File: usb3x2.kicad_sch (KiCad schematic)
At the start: 90 parts

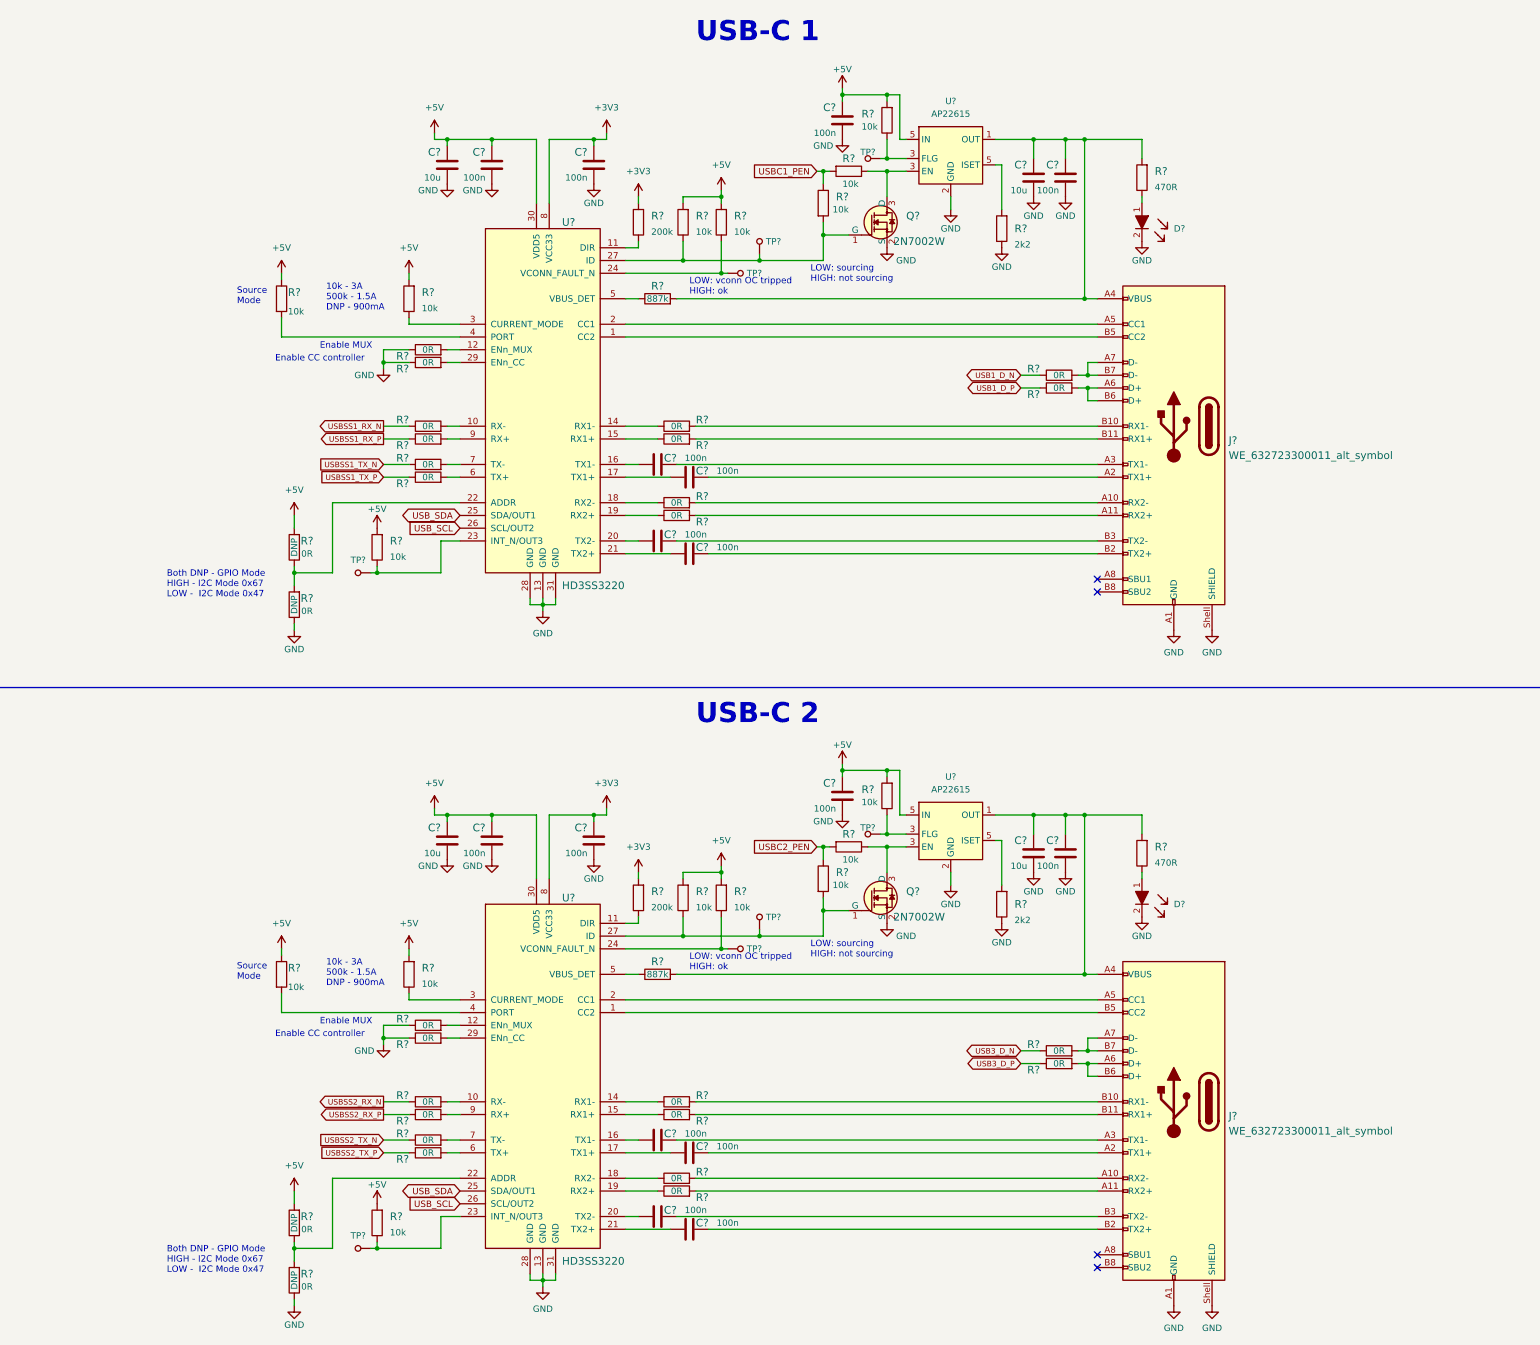
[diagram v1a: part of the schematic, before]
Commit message: Added ESD protection for USB connectors
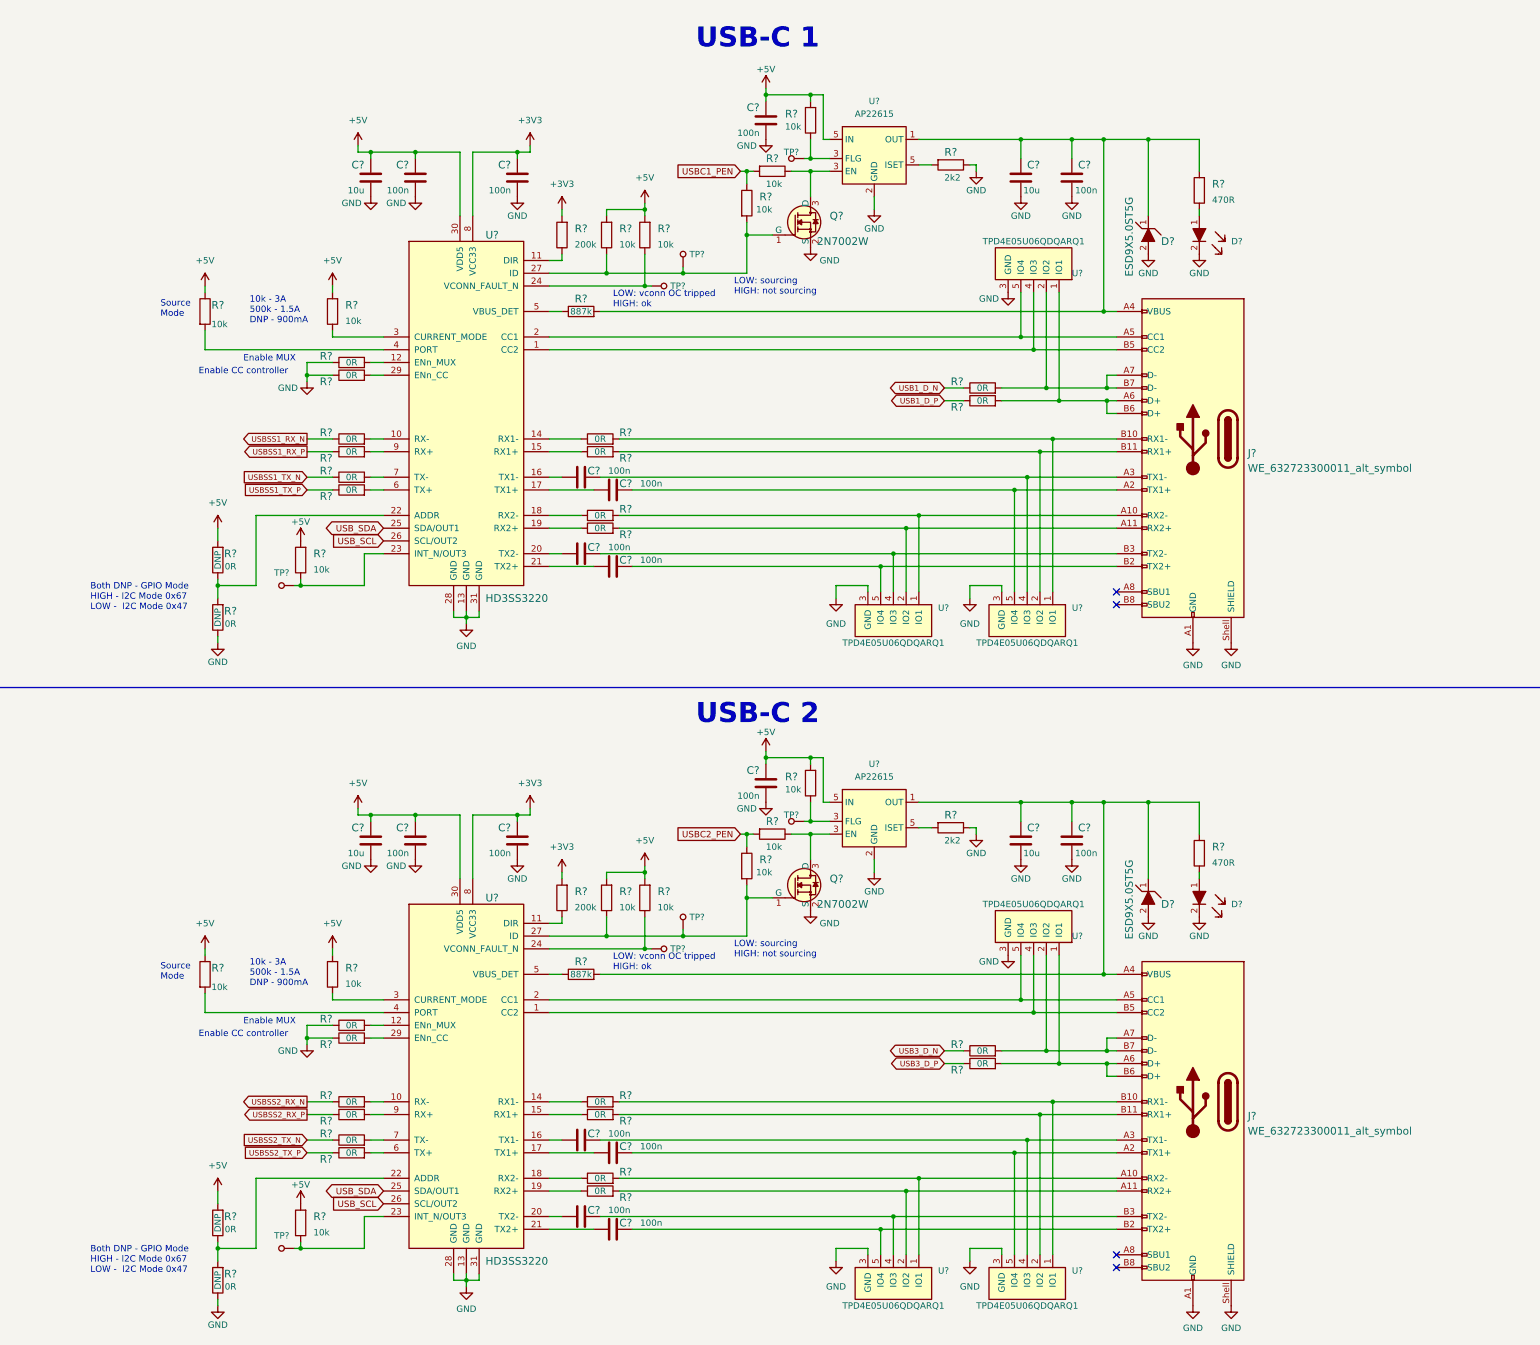
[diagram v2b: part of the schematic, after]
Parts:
- removed C? (x8): C_100n_0402, antmicro-footprints:0402-cap, symbol antmicroCapacitors0402:C_100n_0402
- removed C? (x2): C_10u_0603, antmicro-footprints:0603-cap, symbol antmicroCapacitors0603:C_10u_0603
- removed D?: LTST-C190GKT, crosslink-nx-video-converter-footprints:LED_0603, symbol crosslink-nx-video-converter:LTST-C190GKT
- removed J?: WE_632723300011_alt_symbol, antmicro-footprints:WE_632723300011, symbol antmicroUSBDVIHDMIConnectors:WE_632723300011_alt_symbol
- removed Q?: 2N7002W, antmicro-footprints:SOT-323, symbol antmicroTransistorsFETsMOSFETsSingle: 2N7002W
- removed R? (x8): R_10k_0402, antmicro-footprints:0402-res, symbol antmicroResistors0402:R_10k_0402
- removed R? (x14): R_0R_0402, antmicro-footprints:0402-res, symbol antmicroResistors0402:R_0R_0402
- removed R?: R_470R_0603, antmicro-footprints:0603-res, symbol antmicroResistors0603:R_470R_0603
- removed R?: R_2k2_0402, antmicro-footprints:0402-res, symbol antmicroResistors0402:R_2k2_0402
- removed R?: R_200k_0402, antmicro-footprints:0402-res, symbol antmicroResistors0402:R_200k_0402
- removed R?: R_887k_0402, antmicro-footprints:0402-res, symbol antmicroResistors0402:R_887k_0402
- removed TP? (x4): TP_SMD_0_75MM, antmicro-footprints:Testpoint_smd_0_75mm, symbol antmicroTestPoints:TP_SMD_0_75MM
- removed U?: HD3SS3220, antmicro-footprints:RNH0030A, symbol antmicroInterfaceControllers:HD3SS3220
- removed U?: AP22615, antmicro-footprints:TSOT23-6, symbol antmicroPMICPowerDistributionSwitchesLoadDrivers:AP22615
- added C? (x2): C_10u_0603, antmicro-footprints:0603-cap, symbol antmicroCapacitors0603:C_10u_0603
- added C? (x8): C_100n_0402, antmicro-footprints:0402-cap, symbol antmicroCapacitors0402:C_100n_0402
- added D?: LTST-C190GKT, crosslink-nx-video-converter-footprints:LED_0603, symbol crosslink-nx-video-converter:LTST-C190GKT
- added D? (x2): ESD9X5.0ST5G, antmicro-footprints:SOD-923, symbol antmicroTVSDiodes:ESD9X5.0ST5G
- added J?: WE_632723300011_alt_symbol, antmicro-footprints:WE_632723300011, symbol antmicroUSBDVIHDMIConnectors:WE_632723300011_alt_symbol
- added Q?: 2N7002W, antmicro-footprints:SOT-323, symbol antmicroTransistorsFETsMOSFETsSingle: 2N7002W
- added R? (x14): R_0R_0402, antmicro-footprints:0402-res, symbol antmicroResistors0402:R_0R_0402
- added R?: R_470R_0603, antmicro-footprints:0603-res, symbol antmicroResistors0603:R_470R_0603
- added R? (x8): R_10k_0402, antmicro-footprints:0402-res, symbol antmicroResistors0402:R_10k_0402
- added R?: R_200k_0402, antmicro-footprints:0402-res, symbol antmicroResistors0402:R_200k_0402
- added R?: R_2k2_0402, antmicro-footprints:0402-res, symbol antmicroResistors0402:R_2k2_0402
- added R?: R_887k_0402, antmicro-footprints:0402-res, symbol antmicroResistors0402:R_887k_0402
- added TP? (x4): TP_SMD_0_75MM, antmicro-footprints:Testpoint_smd_0_75mm, symbol antmicroTestPoints:TP_SMD_0_75MM
- added U?: HD3SS3220, antmicro-footprints:RNH0030A, symbol antmicroInterfaceControllers:HD3SS3220
- added U?: AP22615, antmicro-footprints:TSOT23-6, symbol antmicroPMICPowerDistributionSwitchesLoadDrivers:AP22615
- added U? (x6): TPD4E05U06QDQARQ1, antmicro-footprints:TPD4E05U06QDQARQ1, symbol antmicroTVSDiodes:TPD4E05U06QDQARQ1
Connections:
- net +3V3: now also C?.1, R?.2, U?.8 (VCC33)
- net +5V: now also C?.1, C?.1, C?.1, R?.1, R?.2, R?.2, R?.2, R?.2, R?.2, R?.2, U?.30 (VDD5), U?.5 (ISET)
- net GND: now also C?.2, C?.2, C?.2, C?.2, C?.2, C?.2, D?.2, D?.2, D?.2, J?.A1 (GND), J?.A12 (GND), J?.B1 (GND), J?.B12 (GND), J?.Shell (SHIELD), Q?.2 (S), R?.1, R?.1, R?.1, R?.1, U?.13 (GND), U?.2 (GND), U?.28 (GND), U?.3 (GND), U?.3 (GND), U?.3 (GND), U?.3 (GND), U?.3 (GND), U?.3 (GND), U?.31 (GND), U?.8 (GND), U?.8 (GND), U?.8 (GND), U?.8 (GND), U?.8 (GND), U?.8 (GND)
- net USB1_D_N: now also R?.1
- net USB1_D_P: now also R?.1
- net USBC1_PEN: now also R?.1, R?.2
- net USBSS1_RX_N: now also R?.1
- net USBSS1_RX_P: now also R?.1
- net USBSS1_TX_N: now also R?.1
- net USBSS1_TX_P: now also R?.1
- net USB_SCL: now also U?.26 (SCL/OUT2)
- net USB_SDA: now also U?.25 (SDA/OUT1)
- net at C?.1, C?.1, J?.A4 (VBUS)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: now also D?.1
- net at C?.2, J?.B2 (TX2+): now also U?.5 (IO4), U?.6 (IO4)
- net at J?.A7 (D-), J?.B7 (D-), R?.2: now also U?.2 (IO2), U?.9 (IO2)
- net at J?.B5 (CC2), U?.1 (CC2): now also U?.4 (IO3), U?.7 (IO3)
- net at J?.A5 (CC1), U?.2 (CC1): now also U?.5 (IO4), U?.6 (IO4)
- net at C?.2, J?.A2 (TX1+): now also U?.5 (IO4), U?.6 (IO4)
- net at J?.A10 (RX2-), R?.2: now also U?.1 (IO1), U?.10 (IO1)
- net at J?.B11 (RX1+), R?.2: now also U?.2 (IO2), U?.9 (IO2)
- net at C?.2, J?.B3 (TX2-): now also U?.4 (IO3), U?.7 (IO3)
- net at C?.2, J?.A3 (TX1-): now also U?.4 (IO3), U?.7 (IO3)
- net at J?.A11 (RX2+), R?.2: now also U?.2 (IO2), U?.9 (IO2)
- net at J?.A6 (D+), J?.B6 (D+), R?.2: now also U?.1 (IO1), U?.10 (IO1)
- net at J?.B10 (RX1-), R?.2: now also U?.1 (IO1), U?.10 (IO1)
- new net: J?.B5 (CC2), U?.1 (CC2), U?.4 (IO3), U?.7 (IO3)
- new net: R?.2, U?.10 (RX-)
- new net: R?.1, U?.11 (DIR)
- new net: R?.2, U?.12 (ENn_MUX)
- new net: R?.1, U?.14 (RX1-)
- new net: R?.1, U?.15 (RX1+)
- new net: C?.1, U?.16 (TX1-)
- new net: C?.1, U?.17 (TX1+)
- new net: R?.1, U?.18 (RX2-)
- new net: R?.1, U?.19 (RX2+)
- new net: J?.A5 (CC1), U?.2 (CC1), U?.5 (IO4), U?.6 (IO4)
- new net: C?.1, U?.20 (TX2-)
- new net: C?.1, U?.21 (TX2+)
- new net: R?.1, R?.2, U?.22 (ADDR)
- new net: R?.1, TP?.1, U?.23 (INT_N/OUT3)
- new net: R?.1, TP?.1, U?.24 (VCONN_FAULT_N)
- new net: Q?.1 (G), R?.1, R?.2, TP?.1, U?.27 (ID)
- new net: R?.2, U?.29 (ENn_CC)
- new net: R?.1, U?.3 (CURRENT_MODE)
- new net: R?.2, U?.4 (PORT)
- new net: R?.1, U?.5 (VBUS_DET)
- new net: R?.2, U?.6 (TX+)
- new net: R?.2, U?.7 (TX-)
- new net: R?.2, U?.9 (RX+)
- new net: J?.A10 (RX2-), R?.2, U?.1 (IO1), U?.10 (IO1)
- new net: D?.1, R?.1
- new net: C?.1, C?.1, D?.1, J?.A4 (VBUS), J?.A9 (VBUS), J?.B4 (VBUS), J?.B9 (VBUS), R?.2, R?.2, U?.1 (OUT)
- new net: R?.1, TP?.1, U?.3 (FLG)
- new net: Q?.3 (D), R?.1, U?.3 (FLG)
- new net: R?.2, U?.5 (ISET)
- new net: J?.A6 (D+), J?.B6 (D+), R?.2, U?.1 (IO1), U?.10 (IO1)
- new net: C?.2, J?.A2 (TX1+), U?.5 (IO4), U?.6 (IO4)
- new net: J?.A11 (RX2+), R?.2, U?.2 (IO2), U?.9 (IO2)
- new net: C?.2, J?.B3 (TX2-), U?.4 (IO3), U?.7 (IO3)
- new net: C?.2, J?.B2 (TX2+), U?.5 (IO4), U?.6 (IO4)
- new net: C?.2, J?.A3 (TX1-), U?.4 (IO3), U?.7 (IO3)
- new net: J?.A7 (D-), J?.B7 (D-), R?.2, U?.2 (IO2), U?.9 (IO2)
- new net: J?.B10 (RX1-), R?.2, U?.1 (IO1), U?.10 (IO1)
- new net: J?.B11 (RX1+), R?.2, U?.2 (IO2), U?.9 (IO2)
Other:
- moved on the sheet: C?, D?, J?, Q?, R?, TP?, U?

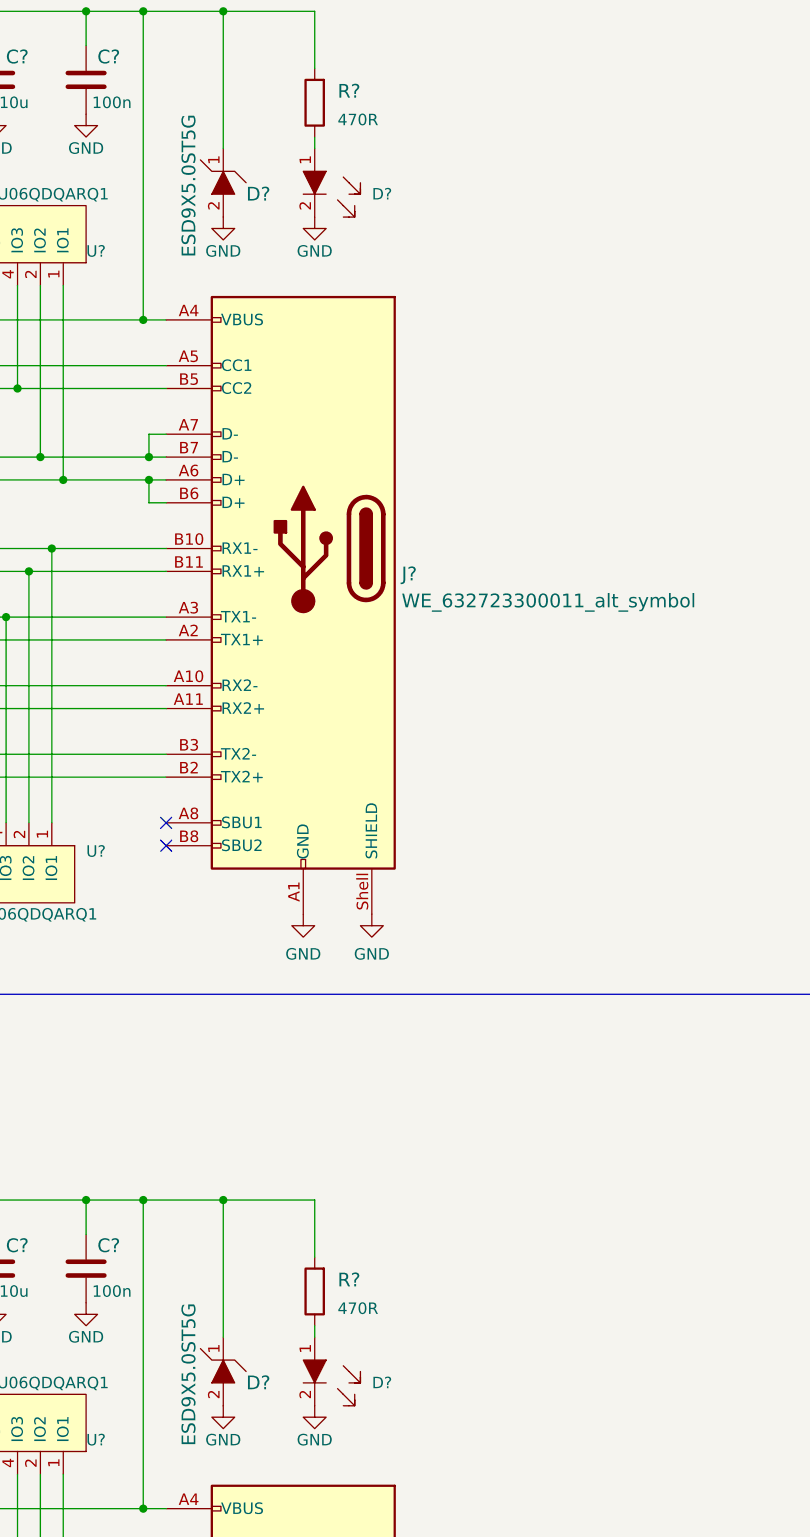
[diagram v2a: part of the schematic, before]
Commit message: Added LED indicators for USB3 and USB0
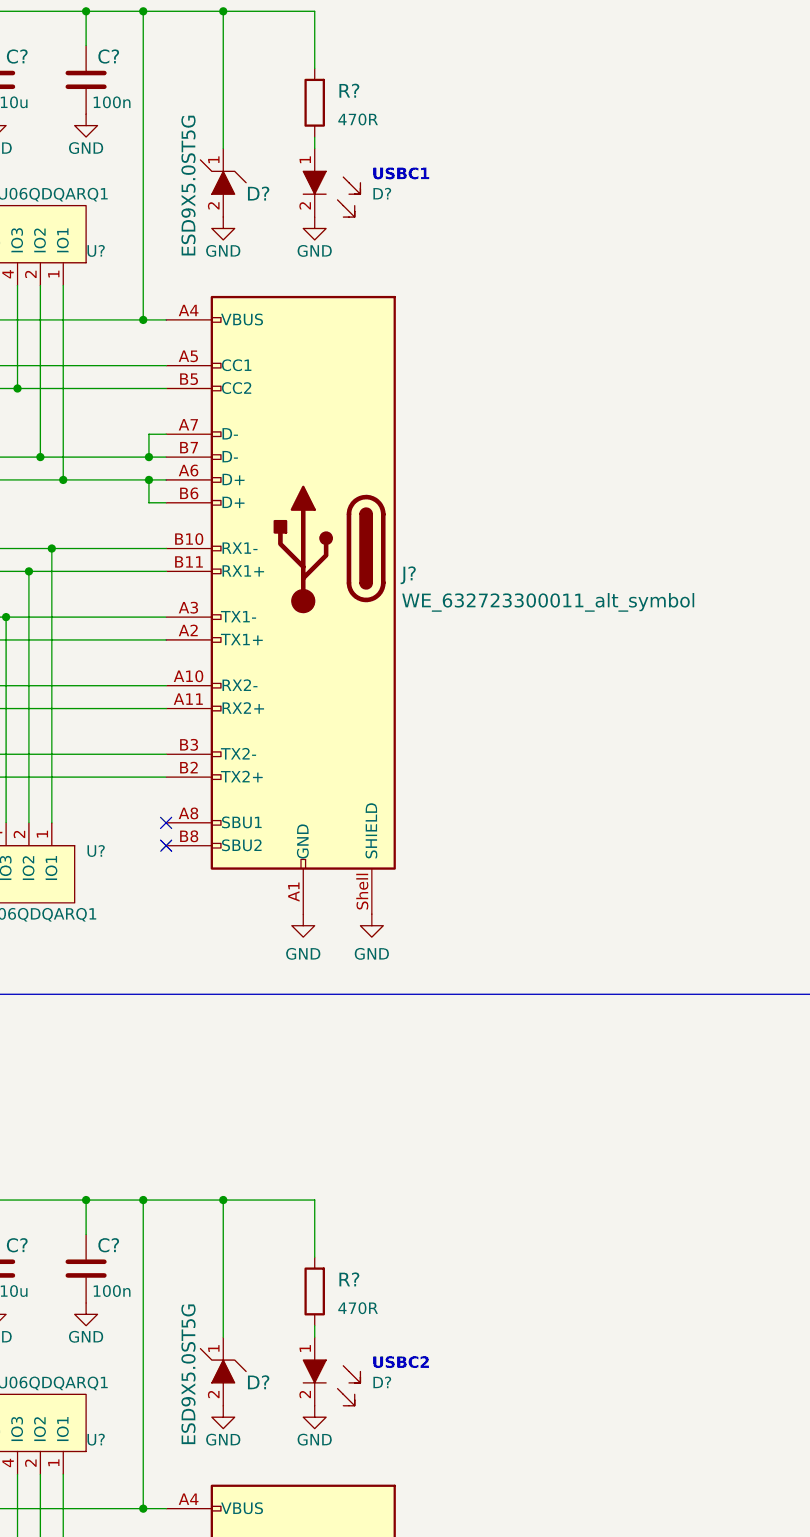
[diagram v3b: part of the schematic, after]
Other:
- note added: "USBC1"
- note added: "USBC2"
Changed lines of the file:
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@@
     (effects (font (size 1.27 1.27)) (justify left bottom))
+  )
+  (text "USBC2" (at 295.91 190.5 0)
+    (effects (font (size 1.27 1.27) (thickness 0.254) bold) (justify left bottom))
+  )
+  (text "USBC1" (at 295.91 58.42 0)
+    (effects (font (size 1.27 1.27) (thickness 0.254) bold) (justify left bottom))
   )
   (text "LOW: vconn OC tripped \nHIGH: ok" (at 172.72 205.105 0)
